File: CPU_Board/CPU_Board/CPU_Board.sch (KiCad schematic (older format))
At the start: 0 parts

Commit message: sd card footprint, step down regler
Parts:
- added C101, C105, C107, C117: 2.2u, Capacitor_SMD:C_1210_3225Metric, symbol Device:C_Small
- added C102, C103: 18p, Capacitor_SMD:C_0603_1608Metric, symbol Device:C_Small
- added C104, C106, C108, C109, C110, C111, C112, C113, C114, C115, C116, C118, C119, C120, C121, C122, C123, C125, C126, C127, C128, C129, C130, C131, C132, C137, C138, C140, C141, C143, C150, C151: 100n, Capacitor_SMD:C_0603_1608Metric, symbol Device:C_Small
- added C124, C133, C134, C135, C136, C139, C142, C144, C145, C146, C147, C148, C149: 10u, Capacitor_SMD:C_0603_1608Metric, symbol Device:C_Small
- added FB101: 70R, Inductor_SMD:L_0603_1608Metric, symbol Device:Ferrite_Bead_Small
- added J101: Screw_Terminal_01x03, TerminalBlock_RND:TerminalBlock_RND_205-00046_1x03_P5.00mm_Horizontal, symbol Connector:Screw_Terminal_01x03
- added J102, J103, J108, J109: Conn_02x01, Connector_PinHeader_2.54mm:PinHeader_1x02_P2.54mm_Vertical, symbol Connector_Generic:Conn_02x01
- added J104: Conn_01x08_Male, Connector_PinHeader_2.54mm:PinHeader_1x08_P2.54mm_Vertical, symbol Connector:Conn_01x08_Male
- added J105: Conn_02x09_Odd_Even, Connector_PinHeader_2.54mm:PinHeader_2x09_P2.54mm_Vertical, symbol Connector_Generic:Conn_02x09_Odd_Even
- added J106: Micro_SD_Card_Det, ProjectFootprints:TF-115-BCP9, symbol PorjectLibrary:TF-115-BCP9
- added J107: Conn_01x06_Male, Connector_PinHeader_2.54mm:PinHeader_1x06_P2.54mm_Vertical, symbol Connector:Conn_01x06_Male
- added J110: Screw_Terminal_01x04, TerminalBlock_RND:TerminalBlock_RND_205-00047_1x04_P5.00mm_Horizontal, symbol Connector:Screw_Terminal_01x04
- added L101, L102: 12u SRN4018, Inductor_SMD:L_Bourns-SRN4018, symbol Device:L_Small
- added R101: DNP, Resistor_SMD:R_0603_1608Metric, symbol Device:R_Small
- added R102, R103, R104, R105, R120, R121, R124, R125: 10K, Resistor_SMD:R_0603_1608Metric, symbol Device:R_Small
- added R106, R107, R108, R109, R110, R111, R130, R132: 1K, Resistor_SMD:R_0603_1608Metric, symbol Device:R_Small
- added R112, R113, R115, R116, R128: 51K, Resistor_SMD:R_0603_1608Metric_Pad1.05x0.95mm_HandSolder, symbol Device:R_Small
- added R114, R117, R118, R119, R122, R123, R126, R127: 22K1, Resistor_SMD:R_0603_1608Metric_Pad1.05x0.95mm_HandSolder, symbol Device:R_Small
- added R129: 88K7, Resistor_SMD:R_0603_1608Metric_Pad1.05x0.95mm_HandSolder, symbol Device:R_Small
- added R131: 100R, Resistor_SMD:R_0603_1608Metric, symbol Device:R_Small
- added SW101: Rotary_Encoder_Switch, Rotary_Encoder:RotaryEncoder_Alps_EC11E-Switch_Vertical_H20mm_CircularMountingHoles, symbol Device:Rotary_Encoder_Switch
- added U101: STM32H730ZB, Package_QFP:LQFP-144_20x20mm_P0.5mm, symbol MCU_ST_STM32H7:STM32H743ZITx
- added U102: W9864G6KH, Package_SO:TSOP-II-54_22.2x10.16mm_P0.8mm, symbol CPU_Board-rescue:W9864G6KH-PorjectLibrary
- added U103, U104: TPS560430, Package_TO_SOT_SMD:SOT-23-6, symbol PorjectLibrary:TPS560430
- added U105: THVD1500, Package_SO:SOIC-8_3.9x4.9mm_P1.27mm, symbol PorjectLibrary:THVD1500
- added Y101: 48MHz, Crystal:Crystal_SMD_3225-4Pin_3.2x2.5mm, symbol Device:Crystal_GND24
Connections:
- net labels added: +24V, +3.3V, +3V3, +5V, A0, A1, A10, A11, A2, A3, A4, A5, A6, A7, A8, A9, BA0, BA1, CAM_D0, CAM_D1, CAM_D2, CAM_D3, CAM_D4, CAM_D5, CAM_D6, CAM_D7, CAM_PWDN, CAM_RESET, DISP_BL, DISP_CD, DISP_CLK, DISP_DC, DISP_DIN, DISP_RST, DQ0, DQ1, DQ10, DQ11, DQ12, DQ13, DQ14, DQ15, DQ2, DQ3, DQ4, DQ5, DQ6, DQ7, DQ8, DQ9, GND, HSYNC, NBL0, NBL1, NRST, PA0, PA1, PA10, PA11, PA12, PA13, PA14, PA15, PA2, PA3, PA4, PA5, PA6, PA7, PA8, PA9, PB0, PB1, PB10, PB11, PB12, PB13, PB14, PB15, PB2, PB3, PB4, PB5, PB6, PB7, PB8, PB9, PC0, PC1, PC10, PC11, PC12, PC13, PC14, PC15, PC2, PC3, PC4, PC5, PC6, PC7, PC8, PC9, PCLK, PD0, PD1, PD10, PD11, PD12, PD13, PD14, PD15, PD2, PD3, PD4, PD5, PD6, PD7, PD8, PD9, PE0, PE1, PE10, PE11, PE12, PE13, PE14, PE15, PE2, PE3, PE4, PE5, PE6, PE7, PE8, PE9, PF0, PF1, PF10, PF11, PF12, PF13, PF14, PF15, PF2, PF3, PF4, PF5, PF6, PF7, PF8, PF9, PG0, PG1, PG10, PG11, PG12, PG13, PG14, PG15, PG2, PG3, PG4, PG5, PG6, PG7, PG8, PG9, PH0, PH1, RS485+, RS485-, R_SWO, Rx, SDCAS, SDCLE, SDCLK, SDNE1, SDNWE, SDRAS, SIOC, SIOD, TX, T_JTCK, T_JTMS, T_NRST, VREF, VSYNC, XCLK
- wire segments 0 -> 444
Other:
- note added: "64Mbit SDRAM\nKompatibel mit IS42S16400J"
- note added: "Decoupling caps"
- note added: "Kompatibel mit STM32F746VETx"
- note added: "OV7670 connector"
- note added: "RS485 Receiver Transmitter"
- note added: "ST-LINK"
- note added: "TODO: Check Symbol"
- note added: "TODO:\nSD-Karte \nStep-Down\nRS422\nDCMI\nEncoder\nSPI-Display"
- note added: "WS2812 LED Stripe"
- note added: "Waveshare 2inch ST7789 Display"

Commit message: alle parts geplaced. kann gerouted werden. LEDs für Status hinzufügen: run, fault, 5v, 3v3
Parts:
- removed C148, C149: 10u, Capacitor_SMD:C_0603_1608Metric, symbol Device:C_Small
- removed C150, C151: 100n, Capacitor_SMD:C_0603_1608Metric, symbol Device:C_Small
- removed R120, R121, R124: 10K, Resistor_SMD:R_0603_1608Metric, symbol Device:R_Small
- added H101, H102, H103, H104: MountingHole_Pad, MountingHole:MountingHole_3.2mm_M3_Pad_Via, symbol Mechanical:MountingHole_Pad
- added J111: Conn_02x09_Odd_Even, Connector_PinHeader_2.54mm:PinHeader_2x09_P2.54mm_Vertical, symbol Connector_Generic:Conn_02x09_Odd_Even
- added R137: 10K, Resistor_SMD:R_0603_1608Metric, symbol Device:R_Small
- C124, C133, C134, C135, C136, C139, C142, C144, C145, C146, C147: footprint Capacitor_SMD:C_0603_1608Metric -> Capacitor_SMD:C_1210_3225Metric
- J104: footprint Connector_PinHeader_2.54mm:PinHeader_1x08_P2.54mm_Vertical -> ProjectFootprints:ST7789_Waveshare
- R112, R113, R114, R115, R116, R117, R118, R119, R122, R123, R126, R127, R128, R129: footprint Resistor_SMD:R_0603_1608Metric_Pad1.05x0.95mm_HandSolder -> Resistor_SMD:R_0603_1608Metric
- U101: symbol MCU_ST_STM32H7:STM32H743ZITx -> PorjectLibrary:STM32H730ZB
- U102: LCSC (none) -> C62378
- U105: value THVD1500 -> ST3485ECDR; LCSC C191014 -> C81185
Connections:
- net labels added: CAM_HSYNC, CAM_PCLK, CAM_SIOC, CAM_SIOD, CAM_VSYNC, CAM_XCLK, RxTx_DIR, SD_CLK, SD_CMD, SD_DAT0, SD_DAT1, SD_DAT2, SD_DAT3, SD_DETECT
- net labels removed: HSYNC, PCLK, SIOC, SIOD, VSYNC, XCLK
- wire segments 444 -> 453
- no-connect marks 0 -> 1
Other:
- note added: "Unused Pins on Pinheader"
- moved on the sheet: C124, C126, C127, C128, C139, C142, C144, C145, C146, C147, J101, J106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

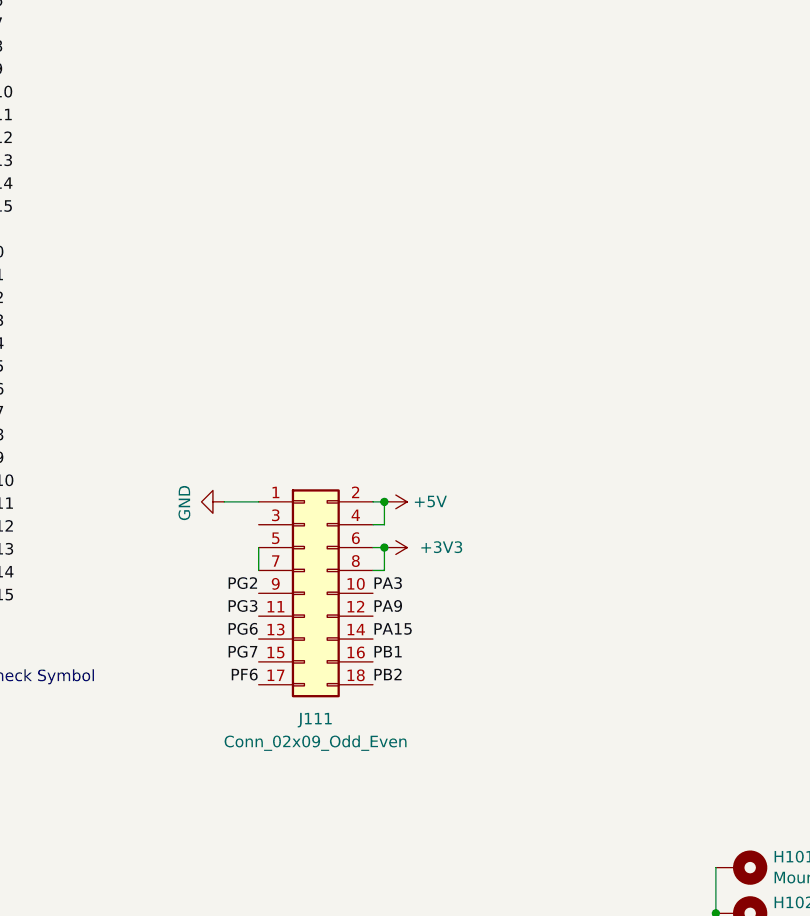
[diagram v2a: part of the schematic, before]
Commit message: ram verdrahtung nicht optimal - noch mal versuchen
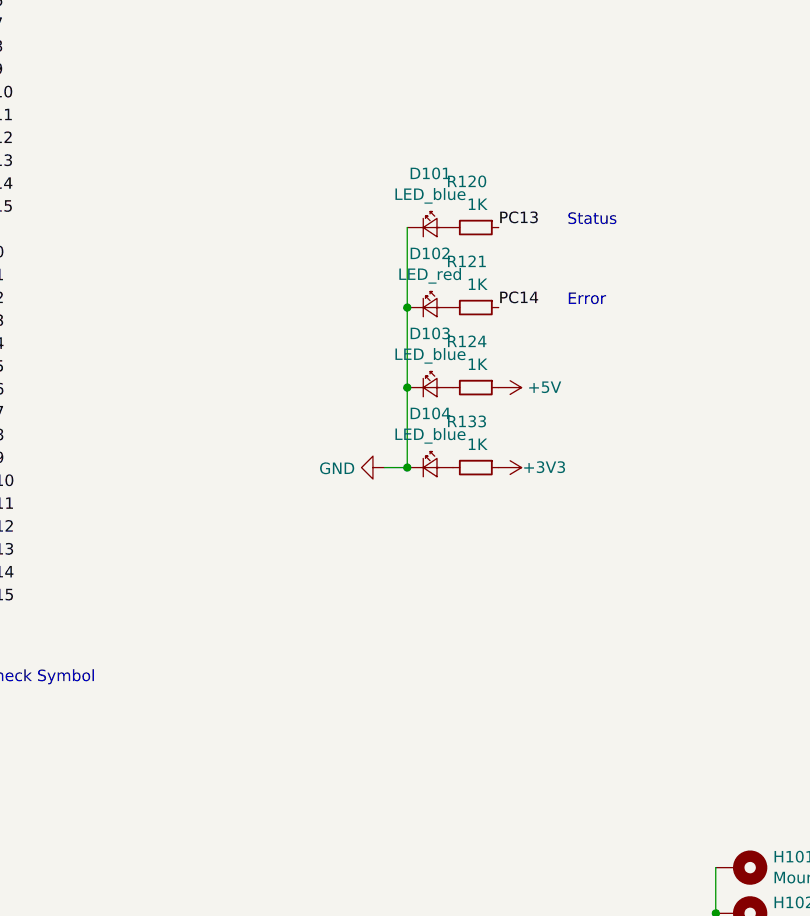
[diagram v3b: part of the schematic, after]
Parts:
- removed J111: Conn_02x09_Odd_Even, Connector_PinHeader_2.54mm:PinHeader_2x09_P2.54mm_Vertical, symbol Connector_Generic:Conn_02x09_Odd_Even
- added D101, D103, D104: LED_blue, LED_SMD:LED_0603_1608Metric, symbol Device:LED_Small
- added D102: LED_red, LED_SMD:LED_0603_1608Metric, symbol Device:LED_Small
- added R120, R121, R124, R133: 1K, Resistor_SMD:R_0603_1608Metric, symbol Device:R_Small
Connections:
- net +3V3: now also R133.1
- net +5V: now also R124.1
- net GND: now also D101.1 (K), D102.1 (K), D103.1 (K), D104.1 (K)
- net PC13: now also R120.1
- net PC14: now also R121.1
- new net: D101.2 (A), R120.2
- new net: D102.2 (A), R121.2
- new net: D103.2 (A), R124.2
- new net: D104.2 (A), R133.2
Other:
- note added: "Error"
- note added: "Status"
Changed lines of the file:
@@
 Wire Wire Line
 	12400 1500 13250 1500
-Text Label 6000 8850 2    50   ~ 0
-PG2
-Text Label 6000 8950 2    50   ~ 0
-PG3
-Text Label 6000 9050 2    50   ~ 0
-PG6
-Text Label 6000 9150 2    50   ~ 0
-PG7
-Text Label 6000 9250 2    50   ~ 0
-PF6
-Text Label 6500 8850 0    50   ~ 0
-PA3
-Text Label 6500 8950 0    50   ~ 0
-PA9
-Text Label 6500 9050 0    50   ~ 0
-PA15
-Text Label 6500 9150 0    50   ~ 0
-PB1
-Text Label 6500 9250 0    50   ~ 0
-PB2
-$Comp
-L power:+3V3 #PWR?
-U 1 1 619410AA
-P 6550 8650
-AR Path="/5FDD0F66/619410AA" Ref="#PWR?"  Part="1"
-AR Path="/619410AA" Ref="#PWR0145"  Part="1"
-F 0 "#PWR0145" H 6550 8500 50  0001 C CNN
-F 1 "+3V3" V 6550 8900 50  0000 C CNN
-F 2 "" H 6550 8650 50  0001 C CNN
-F 3 "" H 6550 8650 50  0001 C CNN
-	1    6550 8650
-	0    1    1    0
-$EndComp
-Wire Wire Line
-	6550 8650 6500 8650
-Wire Wire Line
-	6550 8650 6550 8750
-Wire Wire Line
-	6550 8750 6500 8750
-Connection ~ 6550 8650
-$Comp
-L power:GND #PWR?
-U 1 1 619AB378
-P 5850 8450
-AR Path="/5FDD0F66/619AB378" Ref="#PWR?"  Part="1"
-AR Path="/619AB378" Ref="#PWR0146"  Part="1"
-F 0 "#PWR0146" H 5850 8200 50  0001 C CNN
-F 1 "GND" H 5855 8277 50  0000 C CNN
-F 2 "" H 5850 8450 50  0001 C CNN
-F 3 "" H 5850 8450 50  0001 C CNN
-	1    5850 8450
-	0    1    1    0
-$EndComp
-Wire Wire Line
-	6000 8450 5850 8450
-$Comp
-L power:+5V #PWR?
-U 1 1 61A16A79
-P 6550 8450
-AR Path="/5FDD0F66/61A16A79" Ref="#PWR?"  Part="1"
-AR Path="/61A16A79" Ref="#PWR0156"  Part="1"
-F 0 "#PWR0156" H 6550 8300 50  0001 C CNN
-F 1 "+5V" V 6550 8650 50  0000 C CNN
-F 2 "" H 6550 8450 50  0001 C CNN
-F 3 "" H 6550 8450 50  0001 C CNN
-	1    6550 8450
-	0    1    1    0
-$EndComp
-Wire Wire Line
-	6550 8450 6500 8450
-Wire Wire Line
-	6550 8450 6550 8550
-Wire Wire Line
-	6550 8550 6500 8550
-Connection ~ 6550 8450
 NoConn ~ 6000 10750
 Text Notes 5850 10950 0    50   ~ 0
@@
 $EndComp
 $Comp
-L Connector_Generic:Conn_02x09_Odd_Even J?
-U 1 1 61F4EE38
-P 6200 8850
-AR Path="/5FDD0F66/61F4EE38" Ref="J?"  Part="1"
-AR Path="/61F4EE38" Ref="J111"  Part="1"
-F 0 "J111" H 6250 8300 50  0000 C CNN
-F 1 "Conn_02x09_Odd_Even" H 6250 8200 50  0000 C CNN
-F 2 "Connector_PinHeader_2.54mm:PinHeader_2x09_P2.54mm_Vertical" H 6200 8850 50  0001 C CNN
-F 3 "~" H 6200 8850 50  0001 C CNN
-	1    6200 8850
-	1    0    0    -1
-$EndComp
-Wire Wire Line
-	6000 8650 6000 8750
+L Device:LED_Small D101
+U 1 1 6009F4E1
+P 6750 7250
+F 0 "D101" H 6750 7485 50  0000 C CNN
+F 1 "LED_blue" H 6750 7394 50  0000 C CNN
+F 2 "LED_SMD:LED_0603_1608Metric" V 6750 7250 50  0001 C CNN
+F 3 "~" V 6750 7250 50  0001 C CNN
+F 4 "C193191" H 0   0   50  0001 C CNN "LCSC"
+	1    6750 7250
+	1    0    0    -1
+$EndComp
+$Comp
+L Device:LED_Small D102
+U 1 1 6009FC16
+P 6750 7600
+F 0 "D102" H 6750 7835 50  0000 C CNN
+F 1 "LED_red" H 6750 7744 50  0000 C CNN
+F 2 "LED_SMD:LED_0603_1608Metric" V 6750 7600 50  0001 C CNN
+F 3 "~" V 6750 7600 50  0001 C CNN
+F 4 "C205445" H 0   0   50  0001 C CNN "LCSC"
+	1    6750 7600
+	1    0    0    -1
+$EndComp
+$Comp
+L Device:LED_Small D103
+U 1 1 600D32B0
+P 6750 7950
+F 0 "D103" H 6750 8185 50  0000 C CNN
+F 1 "LED_blue" H 6750 8094 50  0000 C CNN
+F 2 "LED_SMD:LED_0603_1608Metric" V 6750 7950 50  0001 C CNN
+F 3 "~" V 6750 7950 50  0001 C CNN
+F 4 "C193191" H 0   0   50  0001 C CNN "LCSC"
+	1    6750 7950
+	1    0    0    -1
+$EndComp
+$Comp
+L Device:LED_Small D104
+U 1 1 600D339C
+P 6750 8300
+F 0 "D104" H 6750 8535 50  0000 C CNN
+F 1 "LED_blue" H 6750 8444 50  0000 C CNN
+F 2 "LED_SMD:LED_0603_1608Metric" V 6750 8300 50  0001 C CNN
+F 3 "~" V 6750 8300 50  0001 C CNN
+F 4 "C193191" H 0   0   50  0001 C CNN "LCSC"
+	1    6750 8300
+	1    0    0    -1
+$EndComp
+$Comp
+L Device:R_Small R?
+U 1 1 600D3B9A
+P 6950 7250
+AR Path="/5FDD0F66/600D3B9A" Ref="R?"  Part="1"
+AR Path="/600D3B9A" Ref="R120"  Part="1"
+F 0 "R120" V 6750 7300 50  0000 R CNN
+F 1 "1K" V 6850 7300 50  0000 R CNN
+F 2 "Resistor_SMD:R_0603_1608Metric" H 6950 7250 50  0001 C CNN
+F 3 "~" H 6950 7250 50  0001 C CNN
+F 4 "C14676" H 6950 7250 50  0001 C CNN "LCSC"
+	1    6950 7250
+	0    1    1    0
+$EndComp
+$Comp
+L Device:R_Small R?
+U 1 1 600D4954
+P 6950 7600
+AR Path="/5FDD0F66/600D4954" Ref="R?"  Part="1"
+AR Path="/600D4954" Ref="R121"  Part="1"
+F 0 "R121" V 6750 7650 50  0000 R CNN
+F 1 "1K" V 6850 7650 50  0000 R CNN
+F 2 "Resistor_SMD:R_0603_1608Metric" H 6950 7600 50  0001 C CNN
+F 3 "~" H 6950 7600 50  0001 C CNN
+F 4 "C14676" H 6950 7600 50  0001 C CNN "LCSC"
+	1    6950 7600
+	0    1    1    0
+$EndComp
+$Comp
+L Device:R_Small R?
+U 1 1 600D4A46
+P 6950 7950
+AR Path="/5FDD0F66/600D4A46" Ref="R?"  Part="1"
+AR Path="/600D4A46" Ref="R124"  Part="1"
+F 0 "R124" V 6750 8000 50  0000 R CNN
+F 1 "1K" V 6850 8000 50  0000 R CNN
+F 2 "Resistor_SMD:R_0603_1608Metric" H 6950 7950 50  0001 C CNN
+F 3 "~" H 6950 7950 50  0001 C CNN
+F 4 "C14676" H 6950 7950 50  0001 C CNN "LCSC"
+	1    6950 7950
+	0    1    1    0
+$EndComp
+$Comp
+L Device:R_Small R?
+U 1 1 600D4D62
+P 6950 8300
+AR Path="/5FDD0F66/600D4D62" Ref="R?"  Part="1"
+AR Path="/600D4D62" Ref="R133"  Part="1"
+F 0 "R133" V 6750 8350 50  0000 R CNN
+F 1 "1K" V 6850 8350 50  0000 R CNN
+F 2 "Resistor_SMD:R_0603_1608Metric" H 6950 8300 50  0001 C CNN
+F 3 "~" H 6950 8300 50  0001 C CNN
+F 4 "C14676" H 6950 8300 50  0001 C CNN "LCSC"
+	1    6950 8300
+	0    1    1    0
+$EndComp
+$Comp
+L power:GND #PWR0145
+U 1 1 600D5069
+P 6550 8300
+F 0 "#PWR0145" H 6550 8050 50  0001 C CNN
+F 1 "GND" V 6555 8172 50  0000 R CNN
+F 2 "" H 6550 8300 50  0001 C CNN
+F 3 "" H 6550 8300 50  0001 C CNN
+	1    6550 8300
+	0    1    1    0
+$EndComp
+Wire Wire Line
+	6650 7250 6650 7600
+Connection ~ 6650 7600
+Wire Wire Line
+	6650 7600 6650 7950
+Connection ~ 6650 7950
+Wire Wire Line
+	6650 7950 6650 8300
+Wire Wire Line
+	6550 8300 6650 8300
+Connection ~ 6650 8300
+$Comp
+L power:+3V3 #PWR?
+U 1 1 6013C186
+P 7050 8300
+AR Path="/5FDD0F66/6013C186" Ref="#PWR?"  Part="1"
+AR Path="/6013C186" Ref="#PWR0146"  Part="1"
+F 0 "#PWR0146" H 7050 8150 50  0001 C CNN
+F 1 "+3V3" V 7050 8500 50  0000 C CNN
+F 2 "" H 7050 8300 50  0001 C CNN
+F 3 "" H 7050 8300 50  0001 C CNN
+	1    7050 8300
+	0    1    1    0
+$EndComp
+$Comp
+L power:+5V #PWR?
+U 1 1 6013CCB2
+P 7050 7950
+AR Path="/5FDD0F66/6013CCB2" Ref="#PWR?"  Part="1"
+AR Path="/6013CCB2" Ref="#PWR0156"  Part="1"
+F 0 "#PWR0156" H 7050 7800 50  0001 C CNN
+F 1 "+5V" V 7050 8150 50  0000 C CNN
+F 2 "" H 7050 7950 50  0001 C CNN
+F 3 "" H 7050 7950 50  0001 C CNN
+	1    7050 7950
+	0    1    1    0
+$EndComp
+Text Label 7050 7250 0    50   ~ 0
+PC13
+Text Label 7050 7600 0    50   ~ 0
+PC14
+Text Notes 7350 7250 0    50   ~ 0
+Status
+Text Notes 7350 7600 0    50   ~ 0
+Error
 $EndSCHEMATC
